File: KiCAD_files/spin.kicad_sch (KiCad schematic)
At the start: 41 parts, among them J1 OwnTech_SPIN, J5 FTSH-107-01-F-DV-K, J6 USB_C_Receptacle_USB2.0, SW1 PTS815 SJM 250 SMTR LFS, SW2 PTS815 SJM 250 SMTR LFS, T1 Tab, T2 Tab, T3 Tab, T4 Tab, U1 STM32G474RE, U2 AZ1117-33, U3 WE-TVS-82400102, Y1 ECS-240-8-37-CKM-TR3 - 24MHz

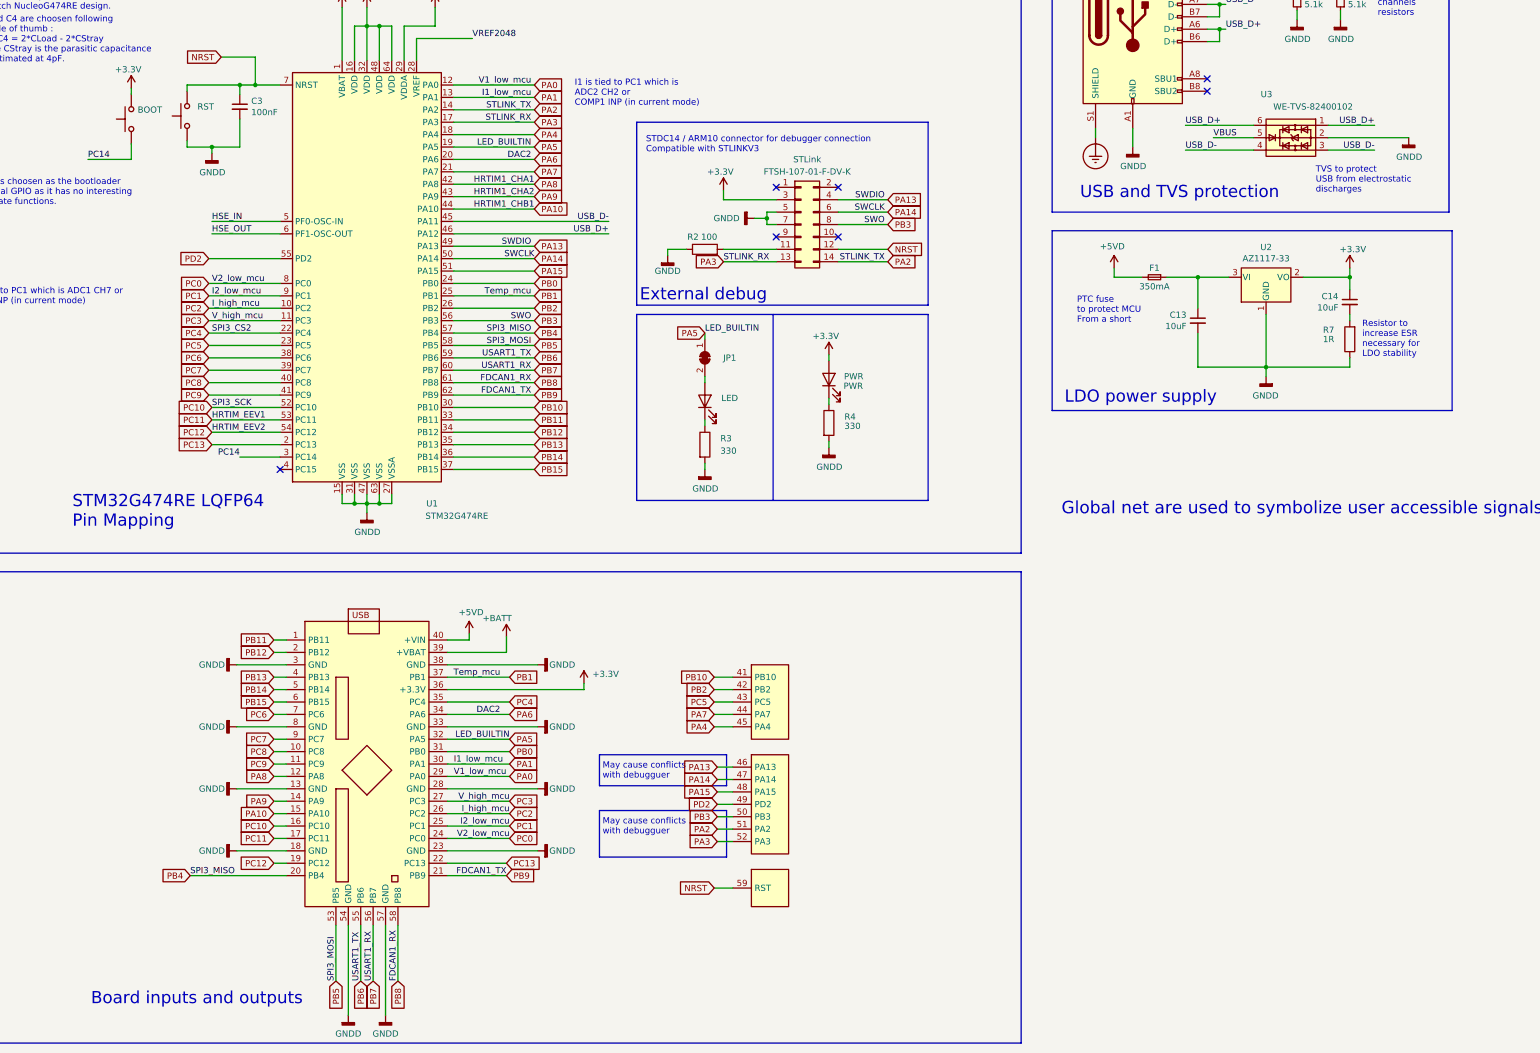
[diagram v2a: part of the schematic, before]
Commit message: Modified Spin footprint
Signed-off-by: Jean Alinei <jean.alinei@laas.fr>
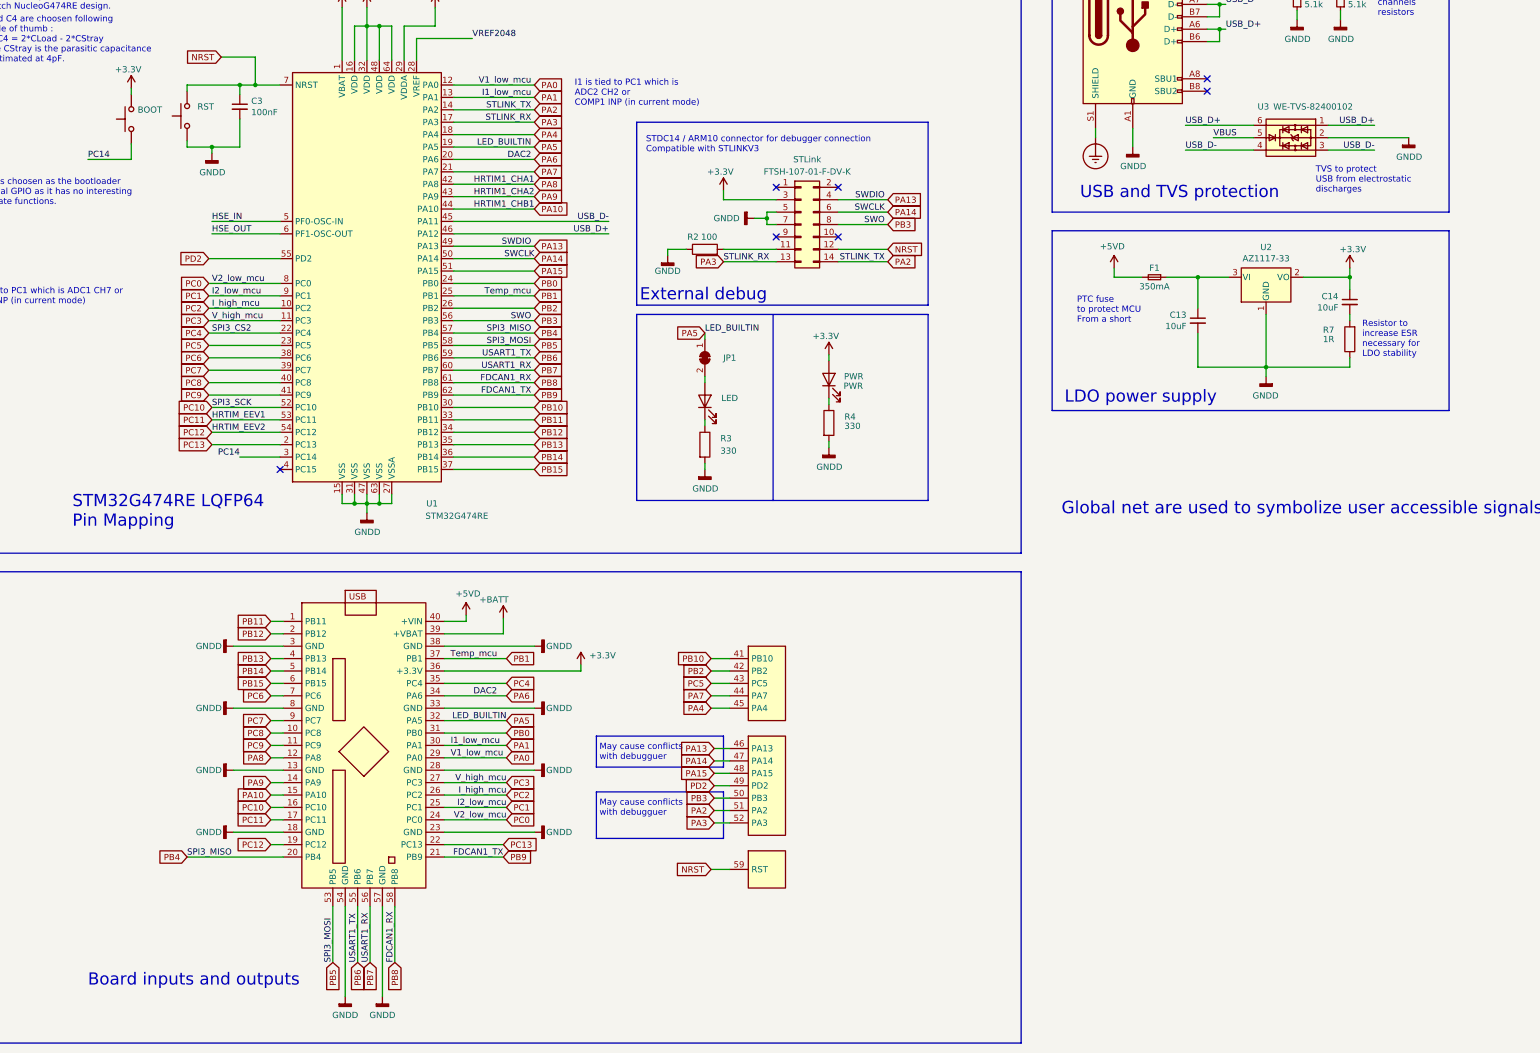
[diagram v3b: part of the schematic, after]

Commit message: rework placement
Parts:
- J6: footprint Connector_USB:USB_C_Receptacle_HRO_TYPE-C-31-M-12 -> Footprints:USB_C_Receptacle_HRO_TYPE-C-31-M-12-reduce-courtyard
- JP1: footprint Resistor_SMD:R_0402_1005Metric -> Jumper:SolderJumper-2_P1.3mm_Bridged_RoundedPad1.0x1.5mm
- renumbered D1 to D
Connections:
- net +5VD_Reg: now reaches C13.1, F1.1, U2.3 (VI)
- net +3V3 renamed +3.3V
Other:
- note added: "USB C configuration channels resistors 5.1k = 500mA max"
- note added: "️May cause conflicts with debugguer"
- note removed: "USB C configuration channels resistors"
- moved on the sheet: C1, C10, C11, C13, C14, C3, C4, C5, C6, C7, C8, C9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

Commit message: big clean is nearly finished
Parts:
- JP1: footprint Jumper:SolderJumper-2_P1.3mm_Bridged_RoundedPad1.0x1.5mm -> Footprints:SolderJumper-2_P1.0mm_Bridged_RoundedPad0.55x1.0mm_small
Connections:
- net +3.3V: now also SW1.1; no longer SW1.2
- net PC14: now also SW1.2; no longer SW1.1
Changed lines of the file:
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@@
       (effects (font (size 1.27 1.27)) hide)
     )
-    (property "Name" "RST" (at 127 85.725 90)
-      (effects (font (size 1.27 1.27)))
+    (property "Name" "RST" (at 124.46 86.36 90)
+      (effects (font (size 1.27 1.27)) (justify right bottom))
     )
     (pin "1")
@@
     )
   )
-  (symbol (lib_id "Switch:SW_Push") (at 111.76 87.63 90) (unit 1)
-    (in_bom yes) (on_board yes) (dnp no)
-    (property "Reference" "SW1" (at 112.9792 86.4616 90)
+  (symbol (lib_id "Switch:SW_Push") (at 111.76 87.63 90) (mirror x) (unit 1)
+    (in_bom yes) (on_board yes) (dnp no)
+    (property "Reference" "SW1" (at 112.9792 88.7984 90)
       (effects (font (size 1.27 1.27)) (justify right) hide)
     )
-    (property "Value" "PTS815 SJM 250 SMTR LFS" (at 112.9792 88.773 90)
+    (property "Value" "PTS815 SJM 250 SMTR LFS" (at 112.9792 86.487 90)
       (effects (font (size 1.27 1.27)) (justify right) hide)
     )
@@
       (effects (font (size 1.27 1.27)) hide)
     )
-    (property "Name" "BOOT" (at 115.57 85.725 90)
-      (effects (font (size 1.27 1.27)))
+    (property "Name" "BOOT" (at 113.03 86.36 90)
+      (effects (font (size 1.27 1.27)) (justify right top))
     )
     (pin "1")
@@
       (effects (font (size 1.27 1.27)) hide)
     )
-    (property "Footprint" "Jumper:SolderJumper-2_P1.3mm_Bridged_RoundedPad1.0x1.5mm" (at 237.49 138.43 0)
-      (effects (font (size 1.27 1.27)) hide)
-    )
+    (property "Footprint" "Footprints:SolderJumper-2_P1.0mm_Bridged_RoundedPad0.55x1.0mm_small" (at 237.49 138.43 0)
+      (effects (font (size 1.27 1.27)) hide)
+    )

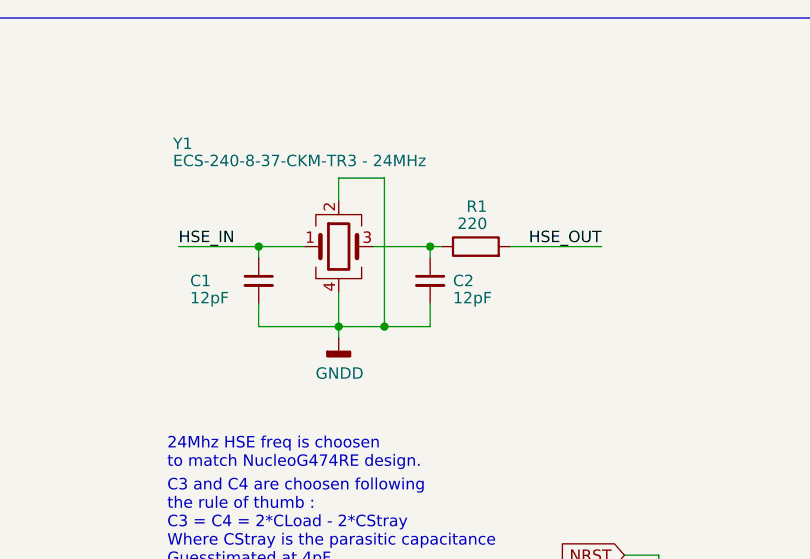
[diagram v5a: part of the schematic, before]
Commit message: updated XTAL
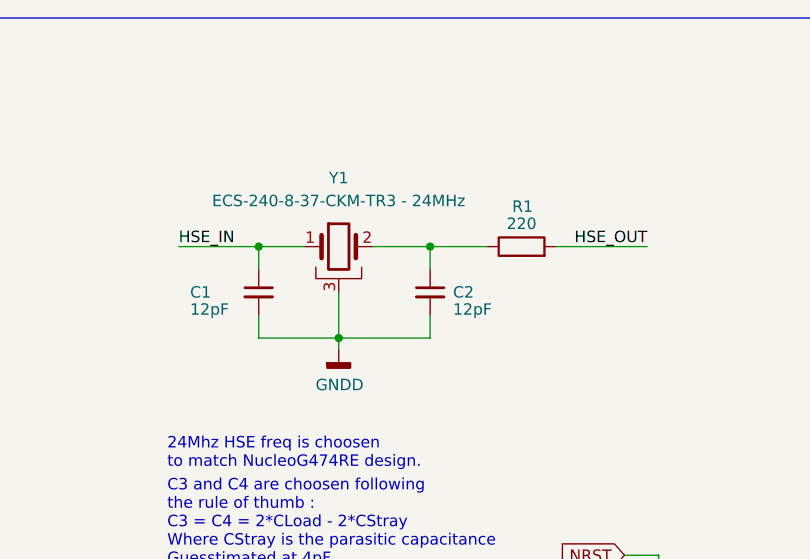
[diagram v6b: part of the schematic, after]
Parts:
- removed Y1: ECS-240-8-37-CKM-TR3 - 24MHz, Crystal:Crystal_SMD_2016-4Pin_2.0x1.6mm, symbol Device:Crystal_GND24
- added Y1: ECS-240-8-37-CKM-TR3 - 24MHz, Footprints:Crystal_SMD_2016-4Pin_ComGnd_2.0x1.6mm, symbol Device:Crystal_GND3
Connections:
- net GNDD: now also Y1.3
- net HSE_IN: now also Y1.1
- net at C2.1, R1.1: now also Y1.2
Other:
- moved on the sheet: C1, C2, R1

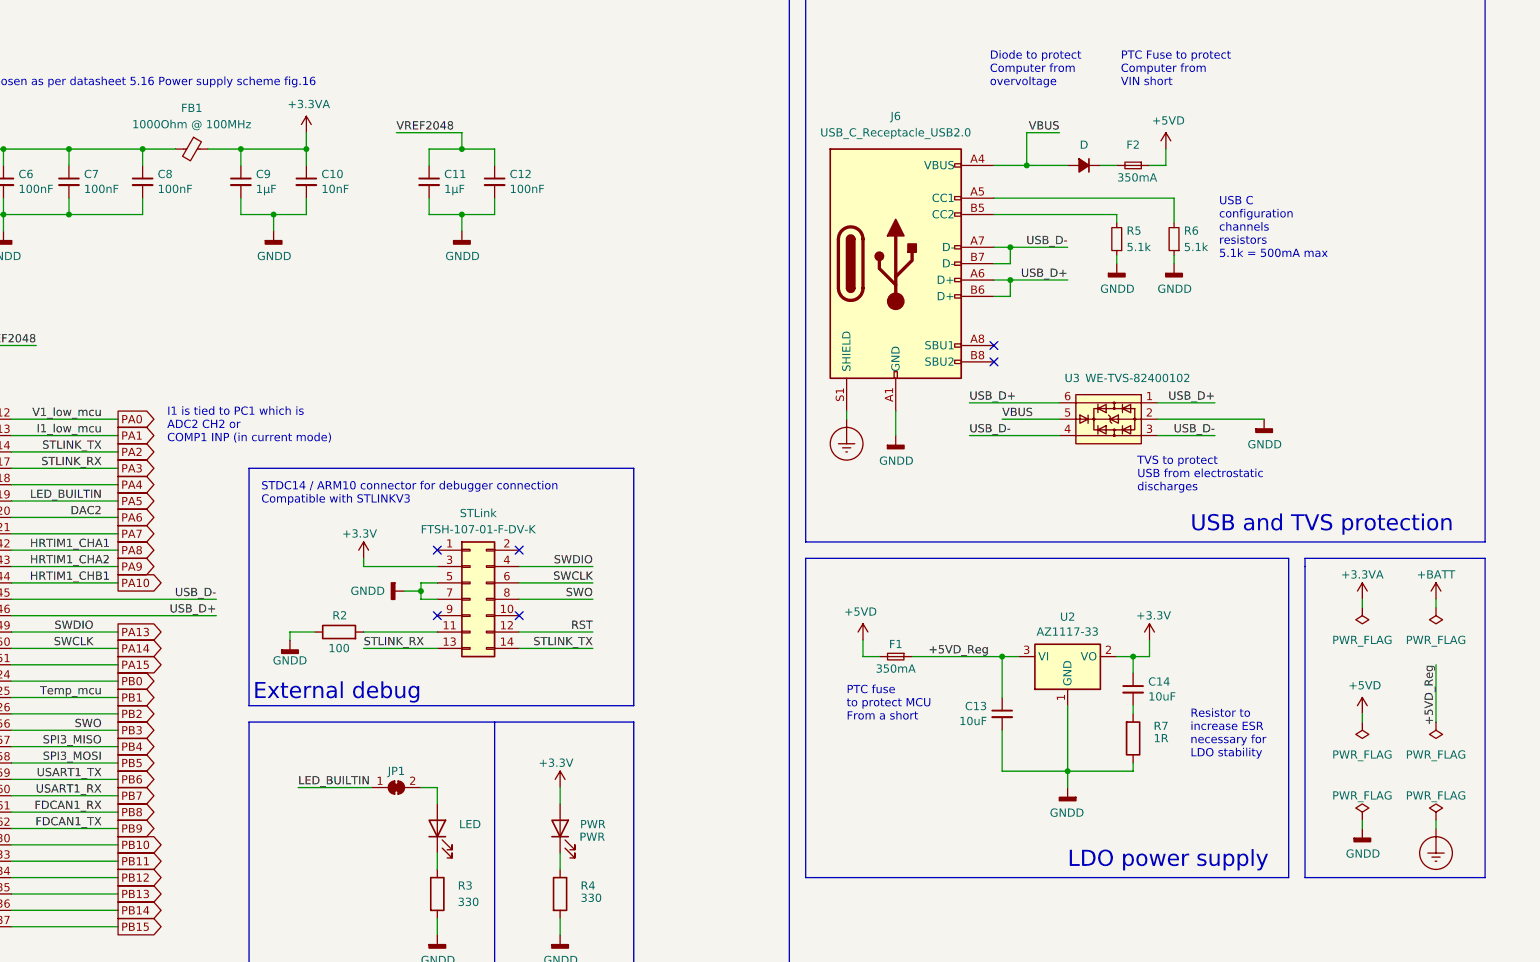
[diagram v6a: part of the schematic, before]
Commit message: fixed manf + 3d model of the crystal
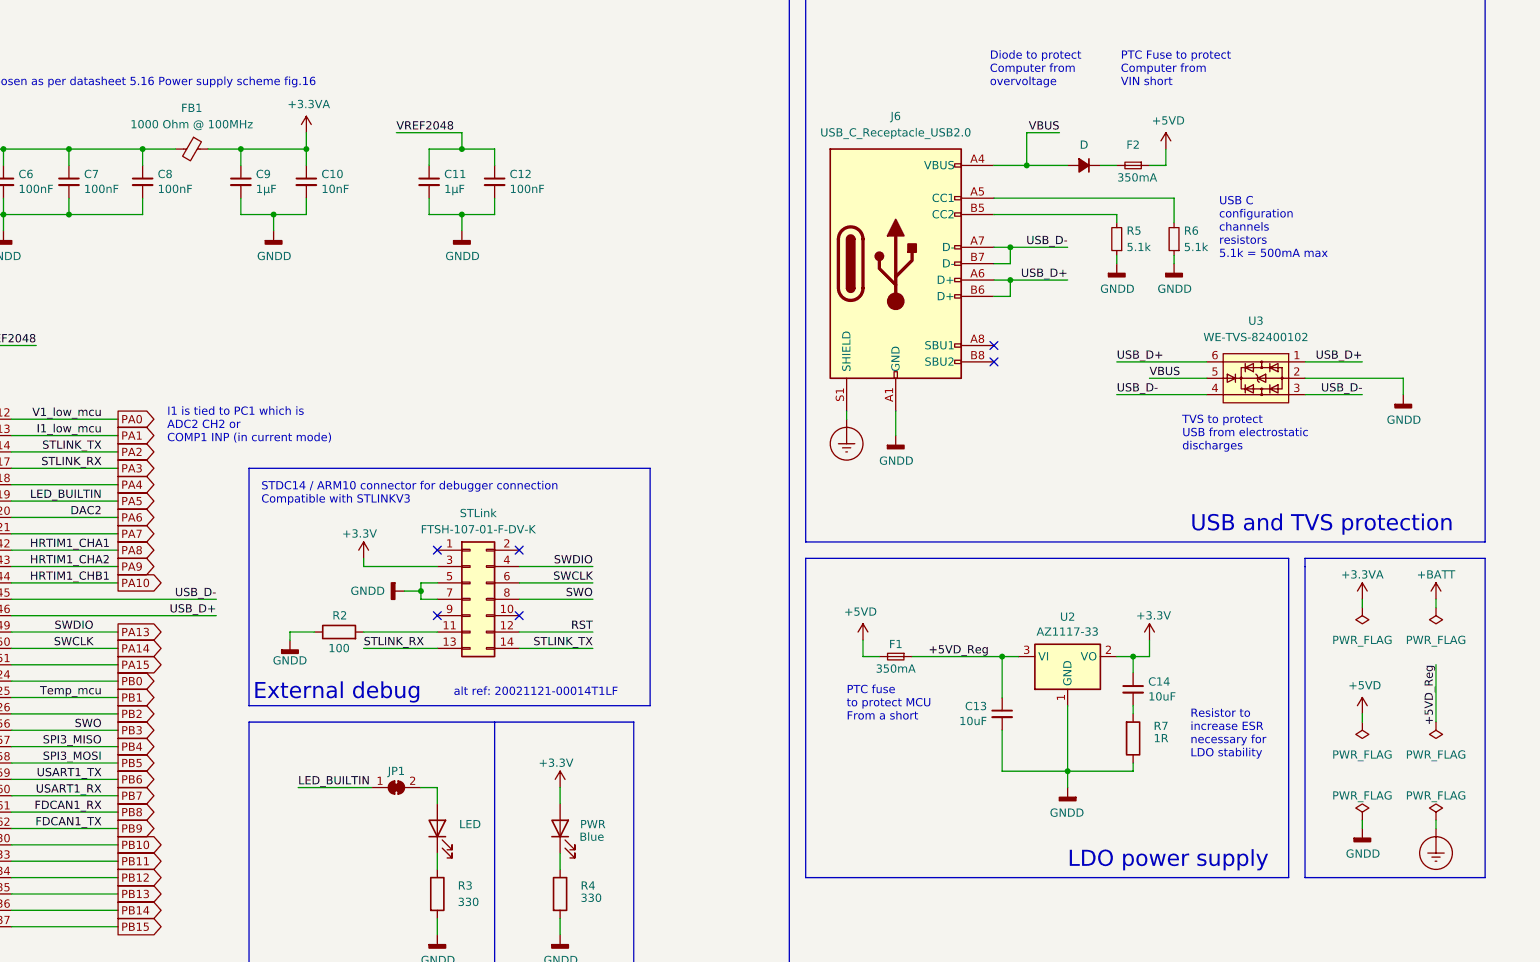
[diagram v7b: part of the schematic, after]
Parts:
- C1, C2: Manf# C0805C120K5HACTU -> C0402C120J5GACTU
- C10: Manf# C0805X103K5RAC3316 -> 0402B103J500CT
- C11, C9: Manf# CL21B105KBFNFNE -> CC0603KRX7R7BB105
- C12, C3, C5, C6, C7, C8: Manf# CC0805KRX7R9BB104 -> VJ0402Y104KXXCW1BC
- C13, C14: Manf# CL32B106KBJZW6E -> CL21B106KAYQNNE
- C4: Manf# CGA4J1X7R1H475K125AE -> GRM188Z71A475ME15D
- FB1: value 1000Ohm @ 100MHz -> 1000 Ohm @ 100MHz; Manf# ILBB0805ER101V -> MFBM1V1005-102-R
- J1: DNP (none) -> x; Manf# (none) -> DNP; now left out of the parts list
- JP1: now left out of the parts list
- LED1: value LED -> Blue; Manf# 150080RS75000 -> 150080BS75000
- LED2: value PWR -> Blue; Manf# 150080RS75000 -> 150080BS75000
- R1: Manf# CRCW0805220RFKEAC -> CR0402-FX-2200GLF
- R2: Manf# CR0805-FX-1000ELF -> AC0402JR-07100RL
- R3, R4: Manf# CRCW0805330RFKEAC -> CRCW0402330RFKEDC
- R5, R6: Footprint-BOM (none) -> 0402; Manf# (none) -> RC0402FR-135K1L
- R7: Manf# CR0805-FX-1000ELF -> RC0402JR-071RL
- SW1, SW2: value PTS815 SJM 250 SMTR LFS -> Push Button
- T1, T2, T3, T4: DNP (none) -> x; Manf# (none) -> DNP
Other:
- note added: "alt ref: 20021121-00014T1LF"
- moved on the sheet: U3
